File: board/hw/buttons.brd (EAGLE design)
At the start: 100 x 68.6 mm, 11 parts

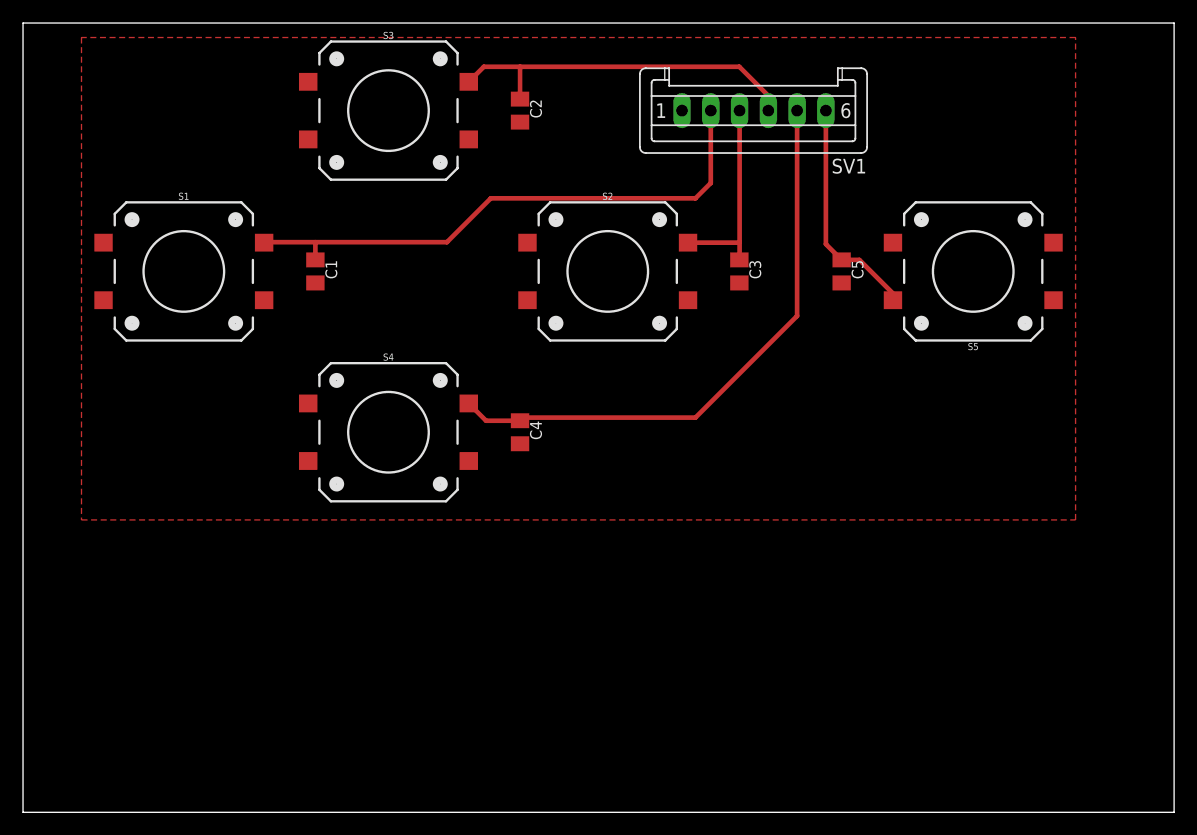
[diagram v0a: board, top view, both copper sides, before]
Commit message: decreased board size to cover only copper part
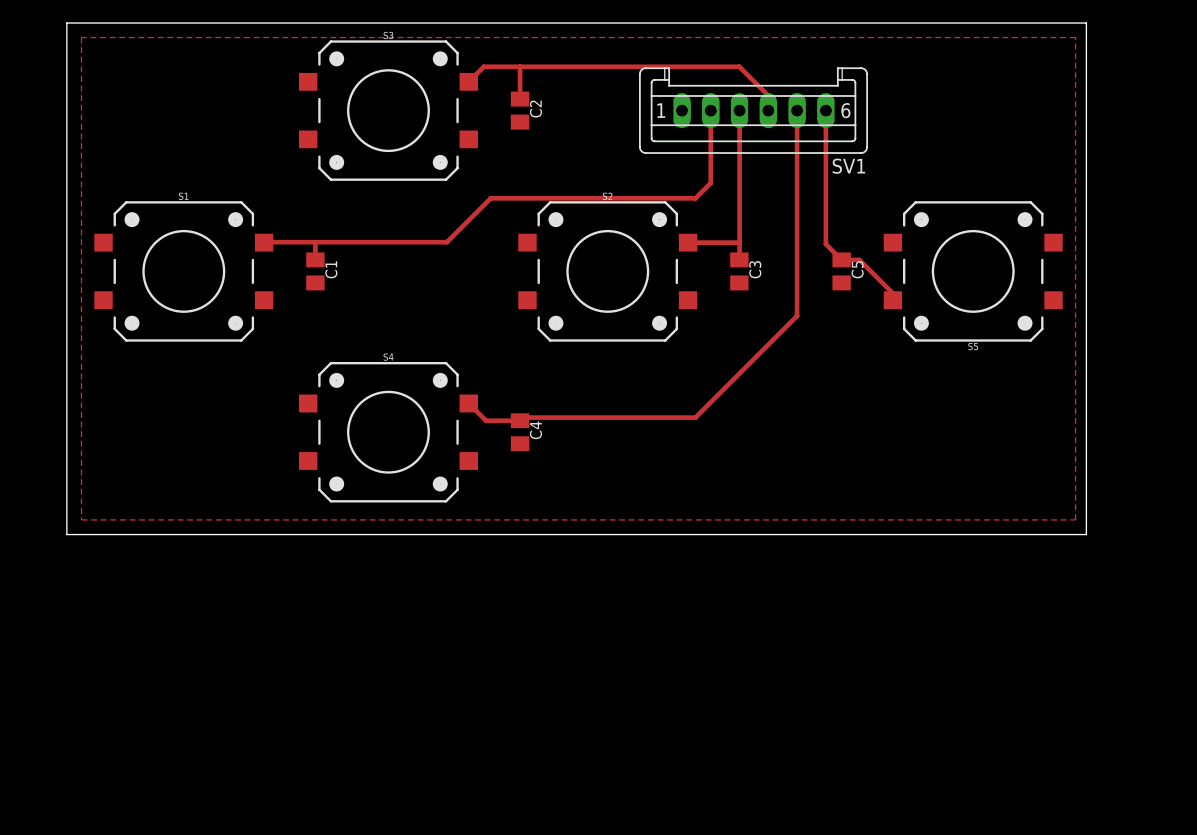
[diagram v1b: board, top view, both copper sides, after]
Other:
- board size 100 x 68.6 mm -> 88.6 x 44.4 mm
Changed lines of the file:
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@@
 <board>
 <plain>
-<wire x1="0" y1="0" x2="100" y2="0" width="0" layer="20"/>
-<wire x1="100" y1="0" x2="100" y2="68.57" width="0" layer="20"/>
-<wire x1="100" y1="68.57" x2="0" y2="68.57" width="0" layer="20"/>
-<wire x1="0" y1="68.57" x2="0" y2="0" width="0" layer="20"/>
+<wire x1="3.81" y1="24.13" x2="92.38" y2="24.13" width="0" layer="20"/>
+<wire x1="92.38" y1="24.13" x2="92.38" y2="68.57" width="0" layer="20"/>
+<wire x1="92.38" y1="68.57" x2="3.81" y2="68.57" width="0" layer="20"/>
+<wire x1="3.81" y1="68.57" x2="3.81" y2="24.13" width="0" layer="20"/>
 </plain>
 <attributes>

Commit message: added 10nF to button boards capacitors
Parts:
- C1, C2, C3, C4, C5: value (none) -> 10nF
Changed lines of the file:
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@@
 <attribute name="OC_NEWARK" value="unknown" x="63.5" y="60.96" size="1.778" layer="27" rot="R180" display="off"/>
 </element>
-<element name="C1" library="rcl" package="C0805K" value="" x="25.4" y="46.99" rot="R270"/>
-<element name="C2" library="rcl" package="C0805K" value="" x="43.18" y="60.96" rot="R270"/>
-<element name="C3" library="rcl" package="C0805K" value="" x="62.23" y="46.99" rot="R270"/>
-<element name="C4" library="rcl" package="C0805K" value="" x="43.18" y="33.02" rot="R270"/>
-<element name="C5" library="rcl" package="C0805K" value="" x="71.12" y="46.99" rot="R270"/>
+<element name="C1" library="rcl" package="C0805K" value="10nF" x="25.4" y="46.99" rot="R270"/>
+<element name="C2" library="rcl" package="C0805K" value="10nF" x="43.18" y="60.96" rot="R270"/>
+<element name="C3" library="rcl" package="C0805K" value="10nF" x="62.23" y="46.99" rot="R270"/>
+<element name="C4" library="rcl" package="C0805K" value="10nF" x="43.18" y="33.02" rot="R270"/>
+<element name="C5" library="rcl" package="C0805K" value="10nF" x="71.12" y="46.99" rot="R270"/>
 </elements>
 <signals>
